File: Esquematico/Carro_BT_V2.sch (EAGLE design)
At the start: 6 parts, among them X2 22-23-2041, X3 22-23-2041, X4 22-23-2021

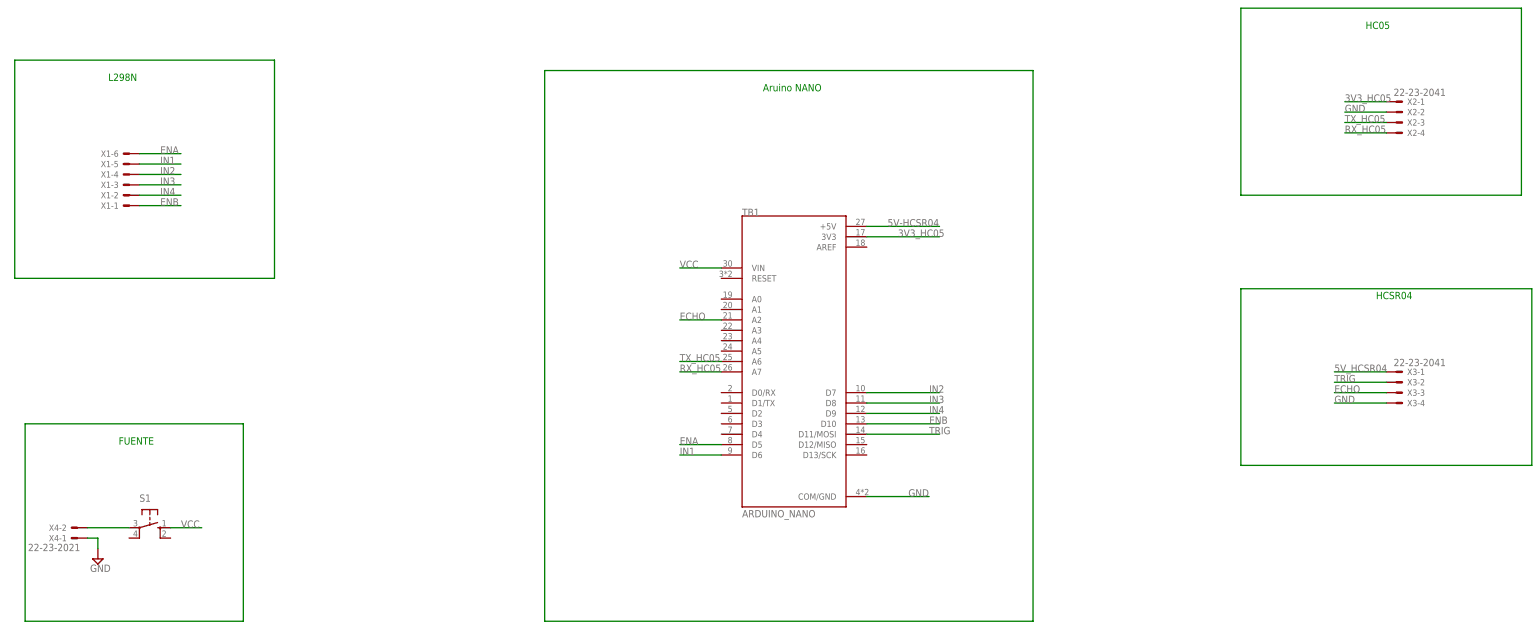
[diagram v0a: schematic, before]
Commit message: Se eliminan las etiquetas del silk screen por problemas en la fabricación, se adicionan mounting holes.
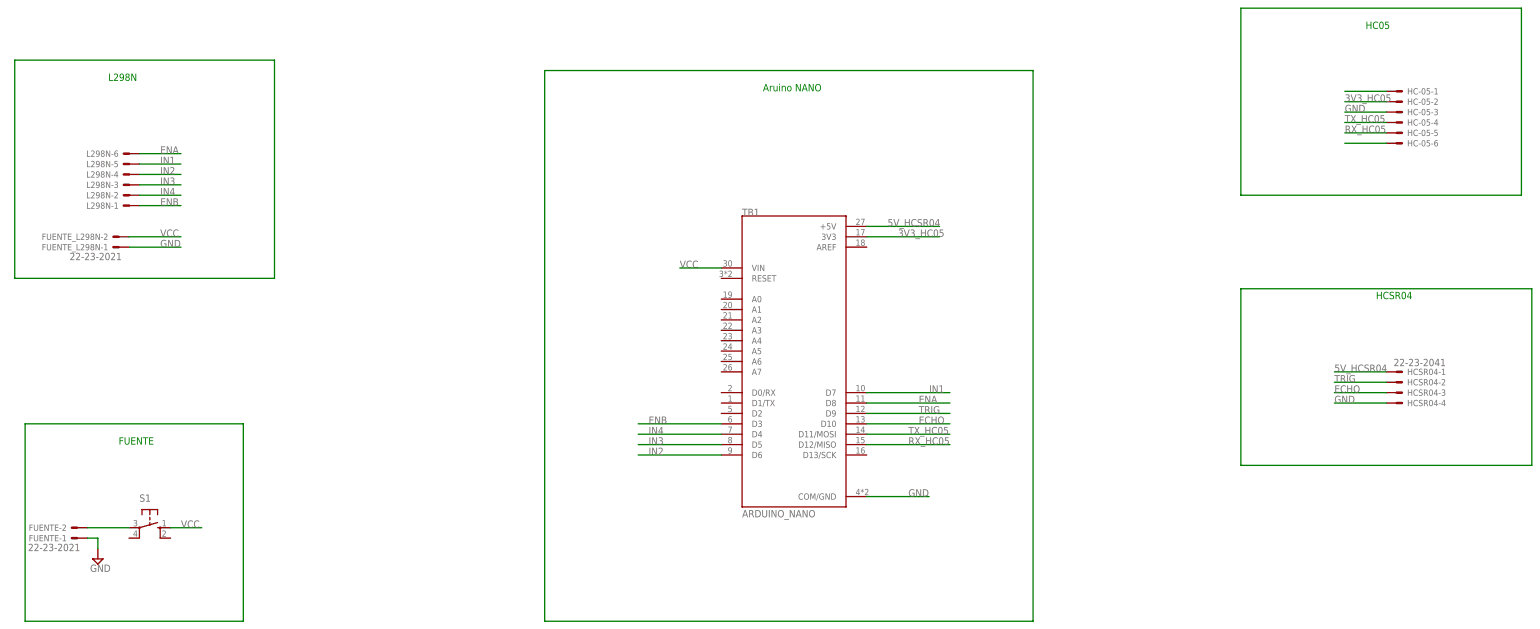
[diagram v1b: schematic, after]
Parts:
- removed X2: 22-23-2041, con-molex:22-23-2041
- added FUENTE_L298N: 22-23-2021, con-molex:22-23-2021
- added HC-05: (no value), con-molex:22-23-2061
- renumbered X1 to L298N, X3 to HCSR04, X4 to FUENTE
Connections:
- removed net 5V-HCSR04: TB1.+5V
- new net ENA1: HC-05-6.S
- new net ENB1: HC-05-1.S
- net 3V3_HC05: now also HC-05-2.S; no longer X2-1.S
- net 5V_HCSR04: now also TB1.+5V
- net ECHO: now also TB1.D10; no longer TB1.A2
- net ENA: now also TB1.D8; no longer TB1.D5
- net ENB: now also TB1.D3; no longer TB1.D10
- net GND: now also FUENTE_L298N-1.S, HC-05-3.S; no longer X2-2.S
- net IN1: now also TB1.D7; no longer TB1.D6
- net IN2: now also TB1.D6; no longer TB1.D7
- net IN3: now also TB1.D5; no longer TB1.D8
- net IN4: now also TB1.D4; no longer TB1.D9
- net RX_HC05: now also HC-05-5.S, TB1.D12/MISO; no longer TB1.A7, X2-4.S
- net TRIG: now also TB1.D9; no longer TB1.D11/MOSI
- net TX_HC05: now also HC-05-4.S, TB1.D11/MOSI; no longer TB1.A6, X2-3.S
- net VCC: now also FUENTE_L298N-2.S
